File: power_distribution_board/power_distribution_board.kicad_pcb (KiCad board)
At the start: 2 copper layers, 144 x 88 mm, 72 parts, among them J1 CONN_01x03, J10 CONN_02X01, J11 CONN_02X01, J12 CONN_02X01, J13 CONN_02X01, J14 CONN_02X01, J15 CONN_02X01, J16 CONN_02X01, J17 CONN_02X01, J18 CONN_02X01, J19 CONN_02X01, J2 CONN_02X01, J20 CONN_02X01, J21 CONN_02X01, J22 CONN_02X01, J23 CONN_02X01, J3 CONN_02X01, J4 CONN_02X01, J5 CONN_02X01, J6 CONN_02X01, J7 CONN_02X01, J8 CONN_02X01, J9 CONN_02X01, Q1 NMOS_SSSGD, Q2 NMOS_SSSGD, Q3 NMOS_SSSGD, Q4 NMOS_SSSGD, Q5 Q_NMOS_GSD, U1 EHHD015A0A, U2 LTC1473, U3 EHHD010A0B, U4 LM317EMP, U5 BTS6133D, U6 A1120

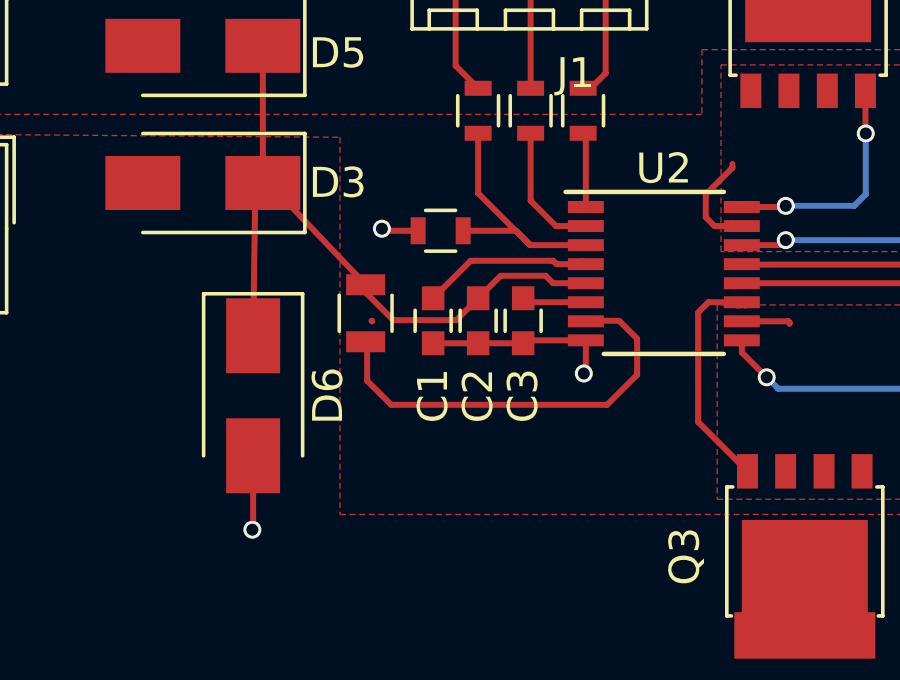
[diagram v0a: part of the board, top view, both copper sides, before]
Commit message: change inductor footprint; update order sheet
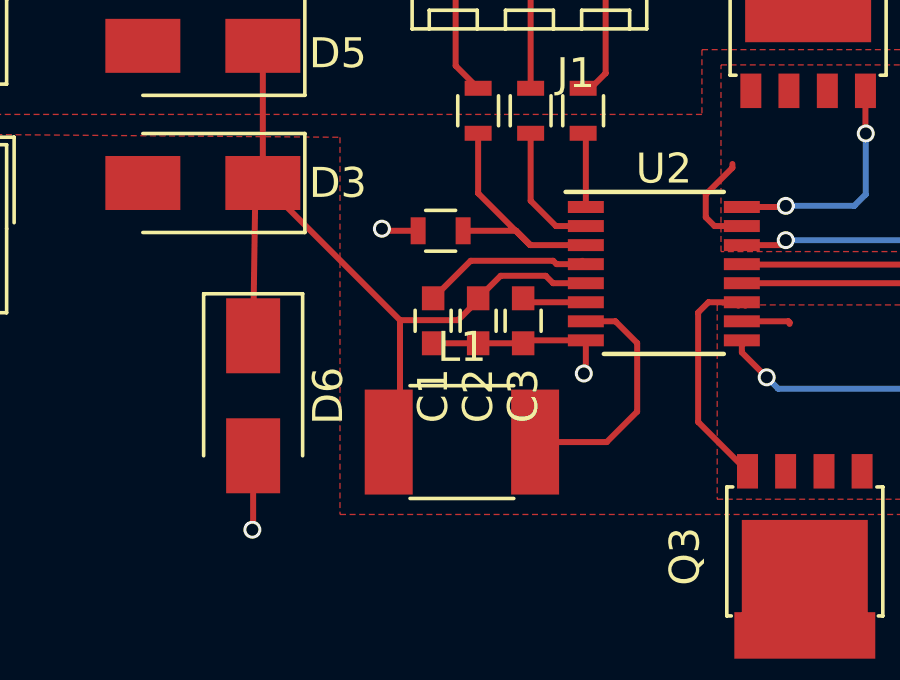
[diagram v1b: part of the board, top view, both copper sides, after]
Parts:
- L1: footprint Inductors_SMD:L_0805 -> Inductors_SMD:L_1812
- moved L1 5.36 mm to (113.5, 138.2), turned to 0 degrees
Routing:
- net Net-(L1-Pad2): track 14.3 -> 8.14 mm
- net Net-(C2-Pad1): track 23.6 -> 27.9 mm

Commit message: final modifications
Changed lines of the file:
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@@
-(kicad_pcb (version 4) (host pcbnew 4.0.7)
+(kicad_pcb (version 4) (host pcbnew 4.0.6)
   (general
     (links 201)
     (no_connects 0)
-    (area 72.924999 60.924999 217.075001 149.075001)
+    (area 72.924999 59.825 217.075001 150.275)
     (thickness 1.6)
     (drawings 9)
@@
     (polygon
       (pts
-        (xy 209.042 149.098) (xy 80.899 149.098) (xy 80.899 60.96) (xy 209.042 60.96)
+        (xy 217 148.138) (xy 73 149) (xy 73 60.862) (xy 217 60)
       )
     )
